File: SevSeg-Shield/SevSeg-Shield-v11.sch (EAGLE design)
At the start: 5 parts, among them U2 ARDUINO_SHIELD

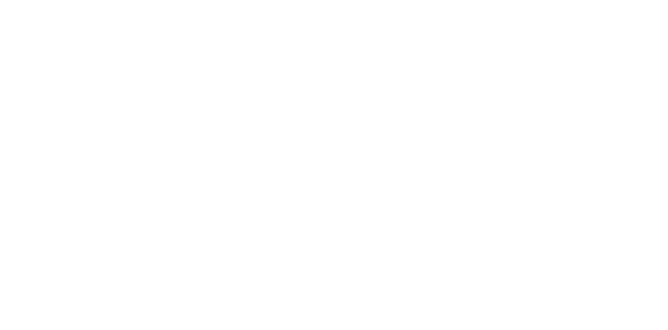
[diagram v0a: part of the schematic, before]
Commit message: Updated the footprint of the display.
Proto worked but the footprint was not quite right. This version should
work a lot better.
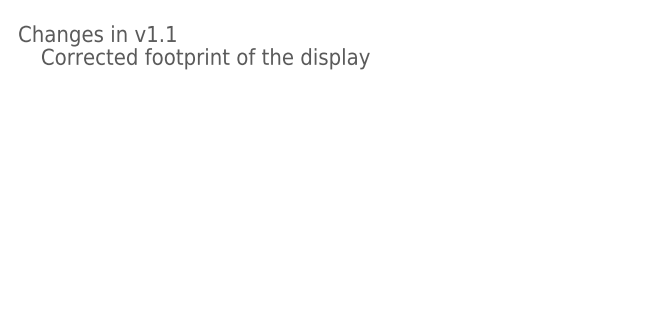
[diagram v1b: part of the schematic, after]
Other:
- note added: "Changes in v1.1"
- note added: "Corrected footprint of the display"
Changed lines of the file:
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@@
 <plain>
 <text x="20.32" y="2.54" size="1.778" layer="97">N. Seidle</text>
+<text x="2.54" y="180.34" size="1.778" layer="97">Changes in v1.1</text>
+<text x="5.08" y="177.8" size="1.778" layer="97">Corrected footprint of the display</text>
 </plain>
 <instances>
